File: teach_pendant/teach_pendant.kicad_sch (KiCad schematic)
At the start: 11 parts, among them J1 Screw_Terminal_01x04, J2 KY-023, J3 KY-023, SW1 SW_Push, SW2 SW_Push, U1 ESP32-DEVKITC-32D, U2 TFT_ILI9488

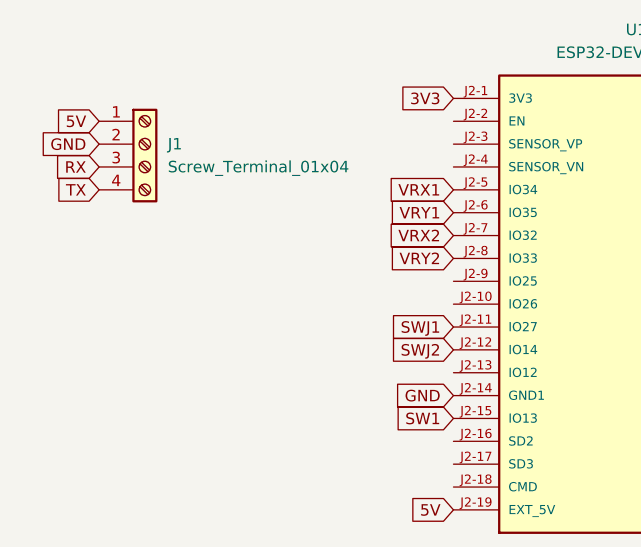
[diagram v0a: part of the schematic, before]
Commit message: agrego funcion boton de paro y librerias necesarias
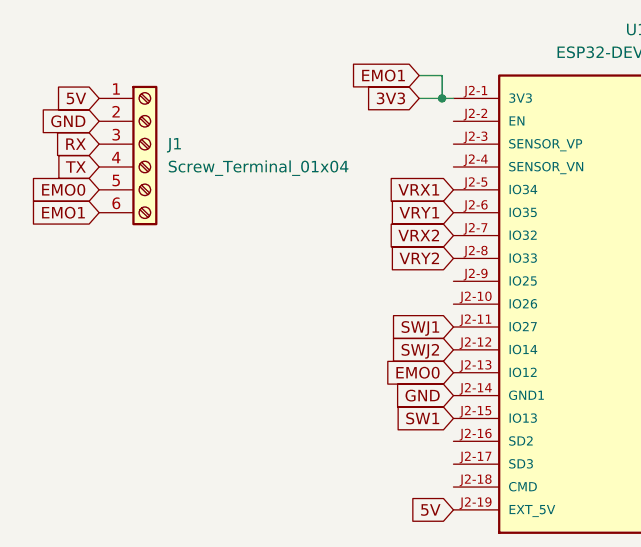
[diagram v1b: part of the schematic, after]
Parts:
- J1: footprint TerminalBlock_Phoenix:TerminalBlock_Phoenix_MKDS-1,5-4-5.08_1x04_P5.08mm_Horizontal -> TerminalBlock_Phoenix:TerminalBlock_Phoenix_MKDS-1,5-6-5.08_1x06_P5.08mm_Horizontal; symbol Connector:Screw_Terminal_01x04 -> Connector:Screw_Terminal_01x06
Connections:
- net 3V3: now also J1.6 (Pin_6)
- net EMO0: now reaches U1.J2-13 (IO12)
- net EMO0: now also J1.5 (Pin_5)
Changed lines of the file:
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@@
   (junction (at 176.53 62.23) (diameter 0) (color 0 0 0 0)
   )
+  (junction (at 127 41.91) (diameter 0) (color 0 0 0 0)
+  )
   (junction (at 177.8 44.45) (diameter 0) (color 0 0 0 0)
   )
@@
     (stroke (width 0) (type default))
   )
+  (wire (pts (xy 127 39.37) (xy 127 41.91))
+    (stroke (width 0) (type default))
+  )
   (wire (pts (xy 176.53 62.23) (xy 180.34 62.23))
     (stroke (width 0) (type default))
   )
+  (wire (pts (xy 127 41.91) (xy 128.27 41.91))
+    (stroke (width 0) (type default))
+  )
   (wire (pts (xy 180.34 41.91) (xy 177.8 41.91))
     (stroke (width 0) (type default))
@@
     (stroke (width 0) (type default))
   )
+  (wire (pts (xy 124.46 41.91) (xy 127 41.91))
+    (stroke (width 0) (type default))
+  )
   (wire (pts (xy 177.8 41.91) (xy 177.8 44.45))
     (stroke (width 0) (type default))
@@
     (stroke (width 0) (type default))
   )
+  (wire (pts (xy 124.46 39.37) (xy 127 39.37))
+    (stroke (width 0) (type default))
+  )
   (wire (pts (xy 176.53 59.69) (xy 176.53 62.23))
     (stroke (width 0) (type default))
   )
+  (global_label "EMO1" (shape input) (at 88.9 54.61 180) (fields_autoplaced)
+    (effects (font (size 1.27 1.27)) (justify right))
+    (property "Intersheetrefs" "${INTERSHEET_REFS}" (at 80.7744 54.61 0)
+      (effects (font (size 1.27 1.27)) (justify right) hide)
+    )
+  )
   (global_label "TCS" (shape input) (at 214.63 69.85 0) (fields_autoplaced)
     (effects (font (size 1.27 1.27)) (justify left))
@@
     )
   )
-  (global_label "3V3" (shape input) (at 128.27 41.91 180) (fields_autoplaced)
-    (effects (font (size 1.27 1.27)) (justify right))
-    (property "Intersheetrefs" "${INTERSHEET_REFS}" (at 121.7772 41.91 0)
+  (global_label "3V3" (shape input) (at 124.46 41.91 180) (fields_autoplaced)
+    (effects (font (size 1.27 1.27)) (justify right))
+    (property "Intersheetrefs" "${INTERSHEET_REFS}" (at 117.9672 41.91 0)
       (effects (font (size 1.27 1.27)) (justify right) hide)
     )
@@
     )
   )
+  (global_label "EMO0" (shape input) (at 88.9 52.07 180) (fields_autoplaced)
+    (effects (font (size 1.27 1.27)) (justify right))
+    (property "Intersheetrefs" "${INTERSHEET_REFS}" (at 80.7744 52.07 0)
+      (effects (font (size 1.27 1.27)) (justify right) hide)
+    )
+  )
   (global_label "SWJ2" (shape input) (at 182.88 133.35 180) (fields_autoplaced)
     (effects (font (size 1.27 1.27)) (justify right))
@@
     )
   )
-  (global_label "RX" (shape input) (at 88.9 49.53 180) (fields_autoplaced)
-    (effects (font (size 1.27 1.27)) (justify right))
-    (property "Intersheetrefs" "${INTERSHEET_REFS}" (at 83.4353 49.53 0)
+  (global_label "RX" (shape input) (at 88.9 46.99 180) (fields_autoplaced)
+    (effects (font (size 1.27 1.27)) (justify right))
+    (property "Intersheetrefs" "${INTERSHEET_REFS}" (at 83.4353 46.99 0)
       (effects (font (size 1.27 1.27)) (justify right) hide)
     )
@@
     )
   )
+  (global_label "EMO1" (shape input) (at 124.46 39.37 180) (fields_autoplaced)
+    (effects (font (size 1.27 1.27)) (justify right))
+    (property "Intersheetrefs" "${INTERSHEET_REFS}" (at 116.3344 39.37 0)
+      (effects (font (size 1.27 1.27)) (justify right) hide)
+    )
+  )
   (global_label "VRY1" (shape input) (at 128.27 54.61 180) (fields_autoplaced)
     (effects (font (size 1.27 1.27)) (justify right))
@@
     )
   )
-  (global_label "TX" (shape input) (at 88.9 52.07 180) (fields_autoplaced)
-    (effects (font (size 1.27 1.27)) (justify right))
-    (property "Intersheetrefs" "${INTERSHEET_REFS}" (at 83.7377 52.07 0)
-      (effects (font (size 1.27 1.27)) (justify right) hide)
-    )
-  )
-  (global_label "5V" (shape input) (at 88.9 44.45 180) (fields_autoplaced)
-    (effects (font (size 1.27 1.27)) (justify right))
-    (property "Intersheetrefs" "${INTERSHEET_REFS}" (at 83.6167 44.45 0)
+  (global_label "TX" (shape input) (at 88.9 49.53 180) (fields_autoplaced)
+    (effects (font (size 1.27 1.27)) (justify right))
+    (property "Intersheetrefs" "${INTERSHEET_REFS}" (at 83.7377 49.53 0)
+      (effects (font (size 1.27 1.27)) (justify right) hide)
+    )
+  )
+  (global_label "5V" (shape input) (at 88.9 41.91 180) (fields_autoplaced)
+    (effects (font (size 1.27 1.27)) (justify right))
+    (property "Intersheetrefs" "${INTERSHEET_REFS}" (at 83.6167 41.91 0)
       (effects (font (size 1.27 1.27)) (justify right) hide)
     )
@@
     )
   )
+  (global_label "EMO0" (shape input) (at 128.27 72.39 180) (fields_autoplaced)
+    (effects (font (size 1.27 1.27)) (justify right))
+    (property "Intersheetrefs" "${INTERSHEET_REFS}" (at 120.1444 72.39 0)
+      (effects (font (size 1.27 1.27)) (justify right) hide)
+    )
+  )
   (global_label "GND" (shape input) (at 214.63 46.99 0) (fields_autoplaced)
     (effects (font (size 1.27 1.27)) (justify left))
@@
     )
   )
-  (global_label "GND" (shape input) (at 88.9 46.99 180) (fields_autoplaced)
-    (effects (font (size 1.27 1.27)) (justify right))
-    (property "Intersheetrefs" "${INTERSHEET_REFS}" (at 82.0443 46.99 0)
+  (global_label "GND" (shape input) (at 88.9 44.45 180) (fields_autoplaced)
+    (effects (font (size 1.27 1.27)) (justify right))
+    (property "Intersheetrefs" "${INTERSHEET_REFS}" (at 82.0443 44.45 0)
       (effects (font (size 1.27 1.27)) (justify right) hide)
     )
@@
     )
   )
-  (symbol (lib_id "Connector:Screw_Terminal_01x04") (at 93.98 46.99 0) (unit 1)
+  (symbol (lib_id "Connector:Screw_Terminal_01x06") (at 93.98 46.99 0) (unit 1)
     (in_bom yes) (on_board yes) (dnp no) (fields_autoplaced)
     (property "Reference" "J1" (at 96.52 46.99 0)
@@
       (effects (font (size 1.27 1.27)) (justify left))
     )
-    (property "Footprint" "TerminalBlock_Phoenix:TerminalBlock_Phoenix_MKDS-1,5-4-5.08_1x04_P5.08mm_Horizontal" (at 93.98 46.99 0)
+    (property "Footprint" "TerminalBlock_Phoenix:TerminalBlock_Phoenix_MKDS-1,5-6-5.08_1x06_P5.08mm_Horizontal" (at 93.98 46.99 0)
       (effects (font (size 1.27 1.27)) hide)
     )
@@
     (pin "2")
     (pin "3")
-    (instances
-      (project "teach_pendant"
+    (pin "6")
+    (pin "5")
+    (instances
+      (project "teach_pendant"
